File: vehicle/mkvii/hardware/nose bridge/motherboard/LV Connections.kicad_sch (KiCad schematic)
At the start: 3 parts, among them J4 CONN_pcie_x1, J5 CONN_pcie_x1, J9 CONN_pcie_x1

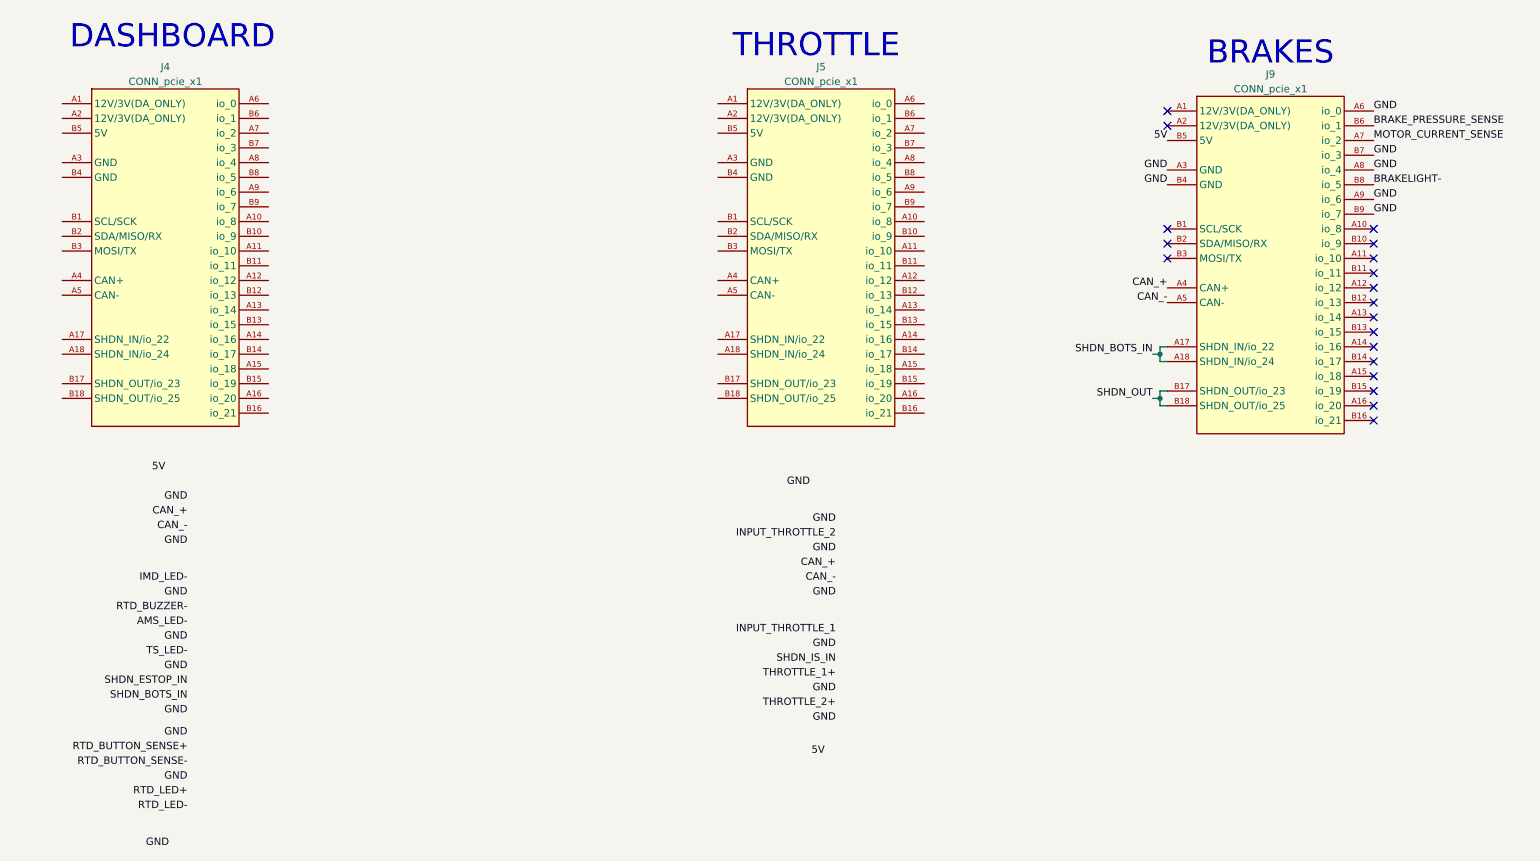
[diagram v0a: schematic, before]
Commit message: Motherboard for MKVII with requested changes and new PCB design.
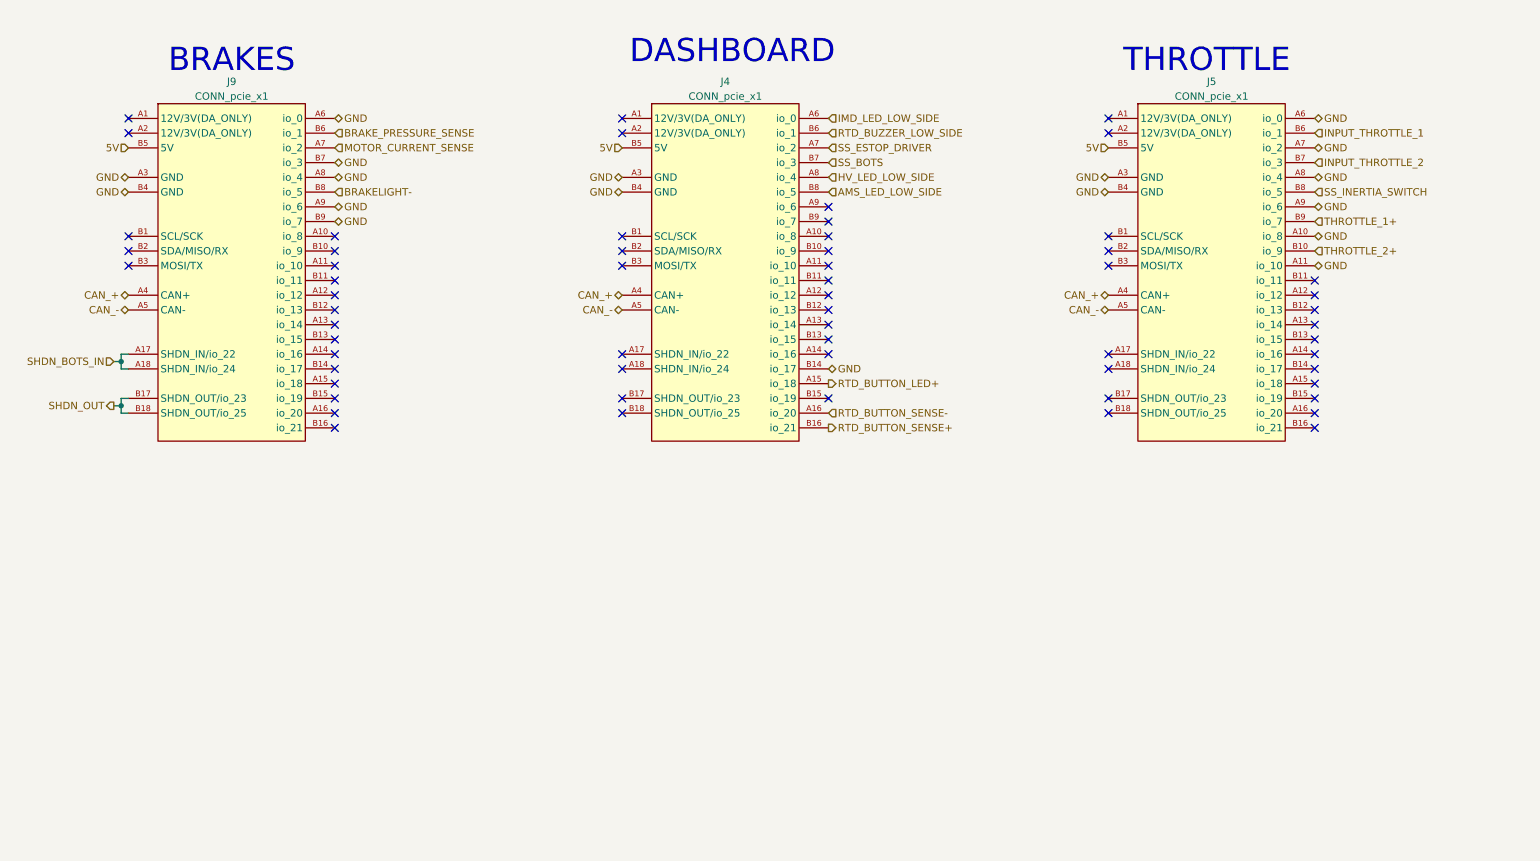
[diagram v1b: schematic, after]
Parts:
- J4, J5, J9: footprint OEM:pcie_x1 -> OEM:te_pcie_x1_connector
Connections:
- net 5V: now also J4.B5 (5V), J5.B5 (5V)
- net CAN_+: now also J4.A4 (CAN+), J5.A4 (CAN+)
- net CAN_-: now also J4.A5 (CAN-), J5.A5 (CAN-)
- net GND: now also J4.A3 (GND), J4.B14 (io_17), J4.B4 (GND), J5.A10 (io_8), J5.A11 (io_10), J5.A3 (GND), J5.A6 (io_0), J5.A7 (io_2), J5.A8 (io_4), J5.A9 (io_6), J5.B4 (GND)
- net INPUT_THROTTLE_1: now also J5.B6 (io_1)
- net INPUT_THROTTLE_2: now also J5.B7 (io_3)
- net RTD_BUTTON_SENSE+: now also J4.B16 (io_21)
- net RTD_BUTTON_SENSE-: now also J4.A16 (io_20)
- net THROTTLE_1+: now also J5.B9 (io_7)
- net THROTTLE_2+: now also J5.B10 (io_9)
- net RTD_BUTTON_LED+: now reaches J4.A15 (io_18)
- net IMD_LED_LOW_SIDE: now reaches J4.A6 (io_0)
- net SS_ESTOP_DRIVER: now reaches J4.A7 (io_2)
- net HV_LED_LOW_SIDE: now reaches J4.A8 (io_4)
- net RTD_BUZZER_LOW_SIDE: now reaches J4.B6 (io_1)
- net SS_BOTS: now reaches J4.B7 (io_3)
- net AMS_LED_LOW_SIDE: now reaches J4.B8 (io_5)
- net SS_INERTIA_SWITCH: now reaches J5.B8 (io_5)
- no-connect marks 19 -> 60
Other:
- moved on the sheet: J4, J5, J9

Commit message: Update for Amanda with new buck converter
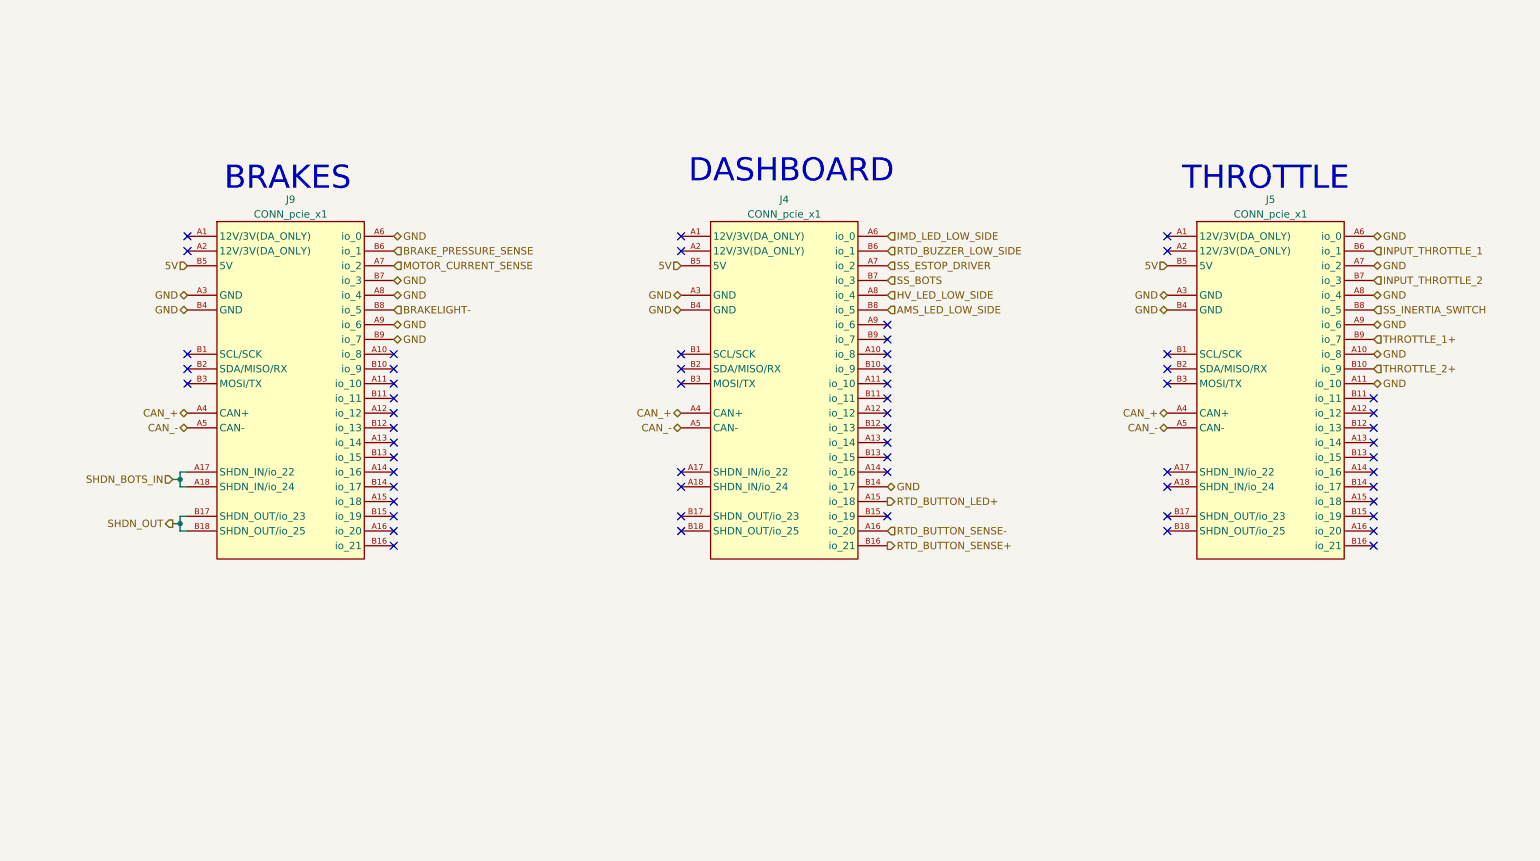
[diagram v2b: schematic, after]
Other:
- moved on the sheet: J4, J5, J9

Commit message: Cleaned up schematics and new PCB layout.
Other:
- company: (none) -> Olin Electric Motorsports
- title: (none) -> Low Voltage Boards Connections
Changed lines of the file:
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@@
 	(paper "A4")
 	(title_block
-		(date "2023-02-14")
+		(title "Low Voltage Boards Connections")
+		(date "2024-12-17")
 		(rev "1")
+		(company "Olin Electric Motorsports")
+		(comment 1 "By Henry Tejada Deras and Ashley Yang")
 	)
 	(junction
